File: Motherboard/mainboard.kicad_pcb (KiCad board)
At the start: 4 copper layers, 45.2 x 36 mm, 46 parts, among them IC1 BMX160, J1 Conn_01x01, J2 10118194-0001LF, J28 Conn_01x01, J29 Conn_01x01, J3 Micro_SD_Card, J30 Conn_01x01, J4 xf2m-2415-1a, J5 XF2M-1015-1A, J6 U.FL-R-SMT-1, J7 U.FL-R-SMT-1, SW1 KMR231NG LFS, U1 RFM95W-915S2, U2 ATSAMD51G_TQFN48, U3 DRV8848, U4 TPS82740BSIPR, U5 DRV8848, U6 MAX708RESA-T, U8 RFM95W-915S2

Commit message: branching for fabrication clean-up and review
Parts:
- removed REF**: U.FL_Hirose_U.FL-R-SMT-1_Vertical, Connector_Coaxial:U.FL_Hirose_U.FL-R-SMT-1_Vertical
- R4, R6: moved to B.Cu
- moved R4 31.4 mm to (80.8, 86.4)
- moved R6 31.3 mm to (80.8, 87.6)

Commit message: placement clean-up
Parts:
- added J8: Conn_01x01, TestPoint:TestPoint_Pad_D1.0mm, F.Cu at (104.6, 118.0)
- C6: moved to F.Cu
- J1, J28, J29, J30: footprint custom-footprints:castellated_small_1side -> TestPoint:TestPoint_Pad_D1.0mm
- R7, R8: moved to B.Cu
- moved R7 15.8 mm to (80.9, 80.1)
- moved SW1 15.1 mm to (87.4, 104.9)
- moved R8 13.7 mm to (80.8, 81.4)
- moved C6 11.3 mm to (95.4, 103.0), turned to 90 degrees
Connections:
- net PA04 renamed Net-(U2-Pad9)
- net PA07 renamed Net-(U2-Pad12)
- net PA21 renamed Net-(U2-Pad30)
- net PA22 renamed Net-(U2-Pad31)
- net PA23 renamed Net-(U2-Pad32)

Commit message: placement getting closer
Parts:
- added FID1: Fiducial, custom-footprints:Fiducial_1mm_Silkscreen, F.Cu at (77.6, 76.1)
- added FID2: Fiducial, custom-footprints:Fiducial_1mm_Silkscreen, F.Cu at (77.6, 107.1)
- added FID3: Fiducial, custom-footprints:Fiducial_1mm_Silkscreen, F.Cu at (120.8, 76.1)
- added FID4: Fiducial, custom-footprints:Fiducial_1mm_Silkscreen, F.Cu at (120.8, 106.6)
- C10, C11, C12, C13, C14, C9, R2, R4, R6, R7, R8: moved to F.Cu
- J4, U6: moved to B.Cu
- moved J30 38.5 mm to (84.6, 93.6)
- moved R5 36.5 mm to (80.0, 95.1), turned to 0 degrees
- moved J28 35.1 mm to (82.0, 96.1)
- moved J29 34.7 mm to (82.0, 93.6)
- moved J1 33.0 mm to (87.1, 96.1)
- moved J8 29.7 mm to (84.6, 96.1)
- moved C10 27.7 mm to (87.4, 89.7)
- moved C11 27.6 mm to (89.6, 89.7)
- moved C9 27.6 mm to (88.5, 89.7)
- moved U3 23.5 mm to (88.6, 89.2), turned to 0 degrees
- moved C12 22.3 mm to (88.7, 82.1), turned to 270 degrees
- moved C13 22.3 mm to (90.1, 82.1), turned to 90 degrees
- moved C14 22.3 mm to (87.3, 82.1), turned to 270 degrees
- moved U5 19.3 mm to (88.5, 82.5)
- moved U6 14.0 mm to (88.8, 103.8), turned to 0 degrees
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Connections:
- net CS_RF1 renamed RF1_CS
- net CS_RF2 renamed RF2_CS
- net Net-(U1-Pad15) renamed RF2_IO1
- net RF_CS renamed Net-(U2-Pad19)
- J4 pad 1: SCL2 -> SDA2
- J4 pad 2: SDA2 -> SCL2
- U2 pad 21: RF_RST -> Net-(U2-Pad21)
- U2 pad 22: RF_BUSY -> Net-(U2-Pad22)
- U2 pad 23: RF_DIO3 -> Net-(U2-Pad23)
- U2 pad 24: CS_CAM -> Net-(U2-Pad24)
- U2 pad 27: CS_IMU -> Net-(U2-Pad27)
- U2 pad 29: EN_CAM -> Net-(U2-Pad29)
- U2 pad 38: RF_DIO2 -> Net-(U2-Pad38)
- U2 pad 39: RF_DIO1 -> Net-(U2-Pad39)
- U2 pad 47: RF_DIO0 -> Net-(U2-Pad47)
- U5 pad 1: MXZ_EN -> MY_EN
- U5 pad 10: MINZ_2 -> Net-(U5-Pad10)
- U5 pad 15: MINX_2 -> MINY_2
- U5 pad 16: MINX_1 -> MINY_1
- U5 pad 2: MINX_1 -> MOY_1
- U5 pad 4: MINX_2 -> MOY_2
- U5 pad 5: MOZ_2 -> Net-(U5-Pad5)
- U5 pad 7: MOZ_1 -> Net-(U5-Pad7)
- U5 pad 8: DXZ_FAULT -> DY_FAULT
- U5 pad 9: MINZ_1 -> Net-(U5-Pad9)
- U8 pad 11: RF_DIO3 -> Net-(U8-Pad11)
- U8 pad 12: RF_BUSY -> RF1_BUSY
- U8 pad 14: RF_DIO0 -> Net-(U8-Pad14)
- U8 pad 15: RF_DIO1 -> RF1_IO1
- U8 pad 16: RF_DIO2 -> Net-(U8-Pad16)
- U8 pad 6: RF_RST -> RF1_RST
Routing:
- net SCL2: track 0.00 -> 15.3 mm, vias 0 -> 2
- net SDA2: track 0.00 -> 15.2 mm, vias 0 -> 2
- net /USB+: track 1.12 -> 12.2 mm, vias 1 -> 2
- net /USB-: track 1.13 -> 12.1 mm, vias 1 -> 2
- net Net-(U2-Pad31): track 0.00 -> 1.56 mm, vias 0 -> 1
- net Net-(U2-Pad27): track 0.00 -> 1.56 mm, vias 0 -> 1
- net Net-(U2-Pad29): track 0.00 -> 1.55 mm, vias 0 -> 1
- net Net-(U2-Pad30): track 0.00 -> 0.80 mm, vias 0 -> 1
- net Net-(U2-Pad28): track 0.00 -> 0.79 mm, vias 0 -> 1
- net Net-(U2-Pad32): track 0.00 -> 0.79 mm, vias 0 -> 1

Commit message: placement roughed-in & routing planned
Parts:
- moved C4 6.87 mm to (113.0, 95.4), turned to 90 degrees
- moved IC1 2.65 mm to (109.0, 95.0)
- moved C2 2.38 mm to (95.3, 104.3)
- moved C8 1.44 mm to (109.0, 98.3), turned to 0 degrees
- moved J5 0.51 mm to (115.1, 98.8)
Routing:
- net SCK: track 0.00 -> 52.8 mm, vias 0 -> 6
- net MISO: track 0.00 -> 46.6 mm, vias 0 -> 6
- net MOSI: track 0.00 -> 46.0 mm, vias 0 -> 6
- net Net-(U2-Pad27): track 1.56 -> 18.6 mm
- net Net-(U2-Pad32): track 0.79 -> 15.7 mm
- net Net-(U2-Pad29): track 1.55 -> 15.1 mm
- net Net-(U2-Pad30): track 0.80 -> 13.4 mm
- net Net-(U2-Pad31): track 1.56 -> 14.1 mm
- net Net-(U2-Pad28): track 0.79 -> 9.97 mm
- net Net-(U2-Pad24): track 0.00 -> 8.29 mm, vias 0 -> 1
- net Net-(U2-Pad21): track 0.00 -> 7.70 mm, vias 0 -> 1
- net Net-(U2-Pad22): track 0.00 -> 4.56 mm, vias 0 -> 1
- net +3V3: track 0.00 -> 3.64 mm, vias 0 -> 5
- net Net-(U2-Pad23): track 0.00 -> 3.32 mm, vias 0 -> 1
- net Net-(U2-Pad16): track 0.00 -> 1.57 mm, vias 0 -> 1
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
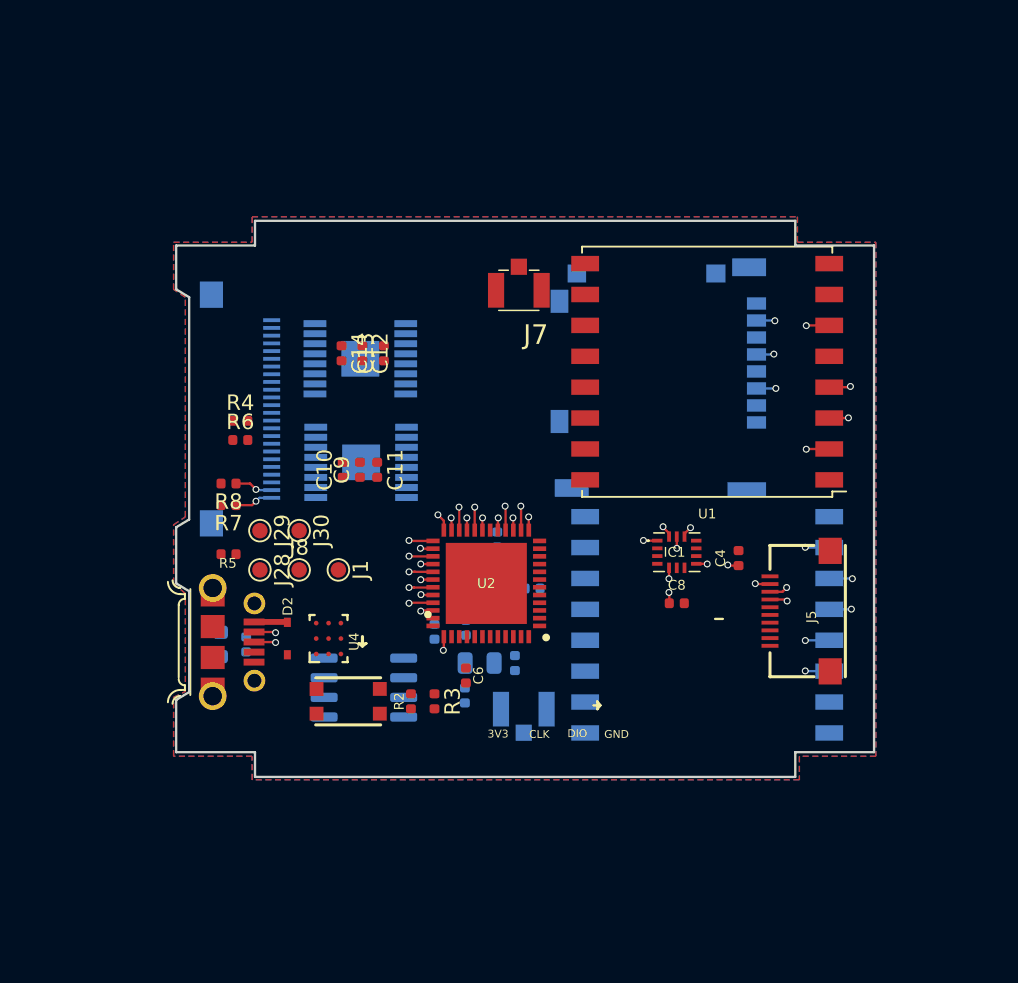
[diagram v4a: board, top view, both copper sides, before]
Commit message: rearranging for power distrobution
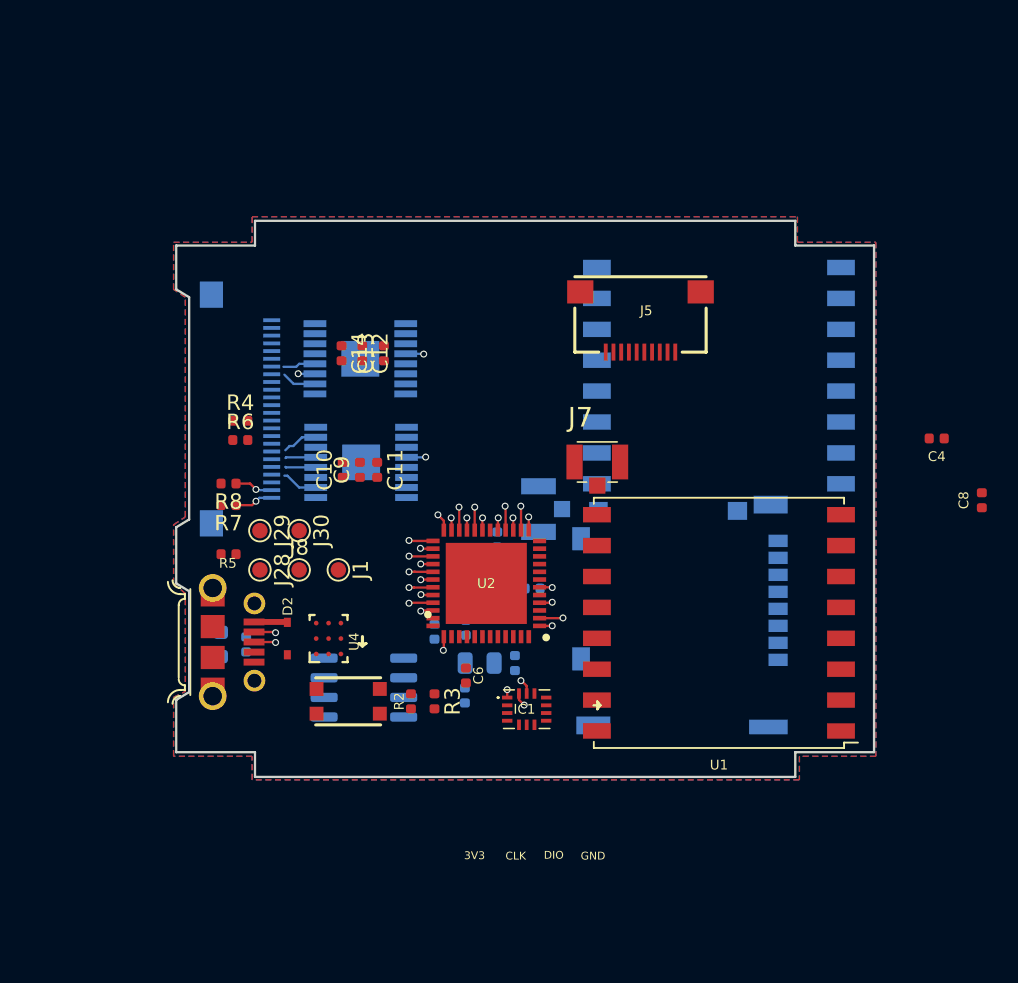
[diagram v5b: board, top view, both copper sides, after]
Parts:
- moved C8 20.8 mm to (128.8, 91.6), turned to 90 degrees
- moved J5 18.7 mm to (106.7, 82.0), turned to 180 degrees
- moved U1 16.3 mm to (111.8, 99.6)
- moved U8 16.1 mm to (111.8, 83.6)
- moved J3 15.4 mm to (110.0, 99.1)
- moved C4 15.0 mm to (125.9, 87.6), turned to 180 degrees
- moved IC1 14.1 mm to (99.3, 105.2)
- moved J6 13.0 mm to (100.1, 92.2), turned to 270 degrees
- moved J7 12.2 mm to (103.9, 89.2), turned to 0 degrees
- moved FID4 5.40 mm to (115.8, 108.7)
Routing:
- net (no net): track 0.00 -> 70.3 mm
- net SCK: track 52.8 -> 13.9 mm, vias 6 -> 2
- net MISO: track 46.6 -> 12.6 mm, vias 6 -> 2
- net MOSI: track 46.0 -> 14.0 mm, vias 6 -> 2
- net BATT_P: track 0.00 -> 17.2 mm, vias 0 -> 2
- net MOX_1: track 0.00 -> 2.34 mm
- net MOZ_1: track 0.00 -> 2.31 mm
- net MOY_1: track 0.00 -> 2.22 mm
- net MOY_2: track 0.00 -> 2.12 mm
- net MOZ_2: track 0.00 -> 1.98 mm
- net MOX_2: track 0.00 -> 1.98 mm
- net RF1_CS: track 1.56 -> 0.00 mm, vias 1 -> 0
- net RF1_RST: track 1.56 -> 0.00 mm, vias 1 -> 0
- net SCL1: track 0.00 -> 1.52 mm, vias 0 -> 1
- net RF2_RST: track 1.49 -> 0.00 mm, vias 1 -> 0
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
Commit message: much cleaner SPI and BATT_P layout
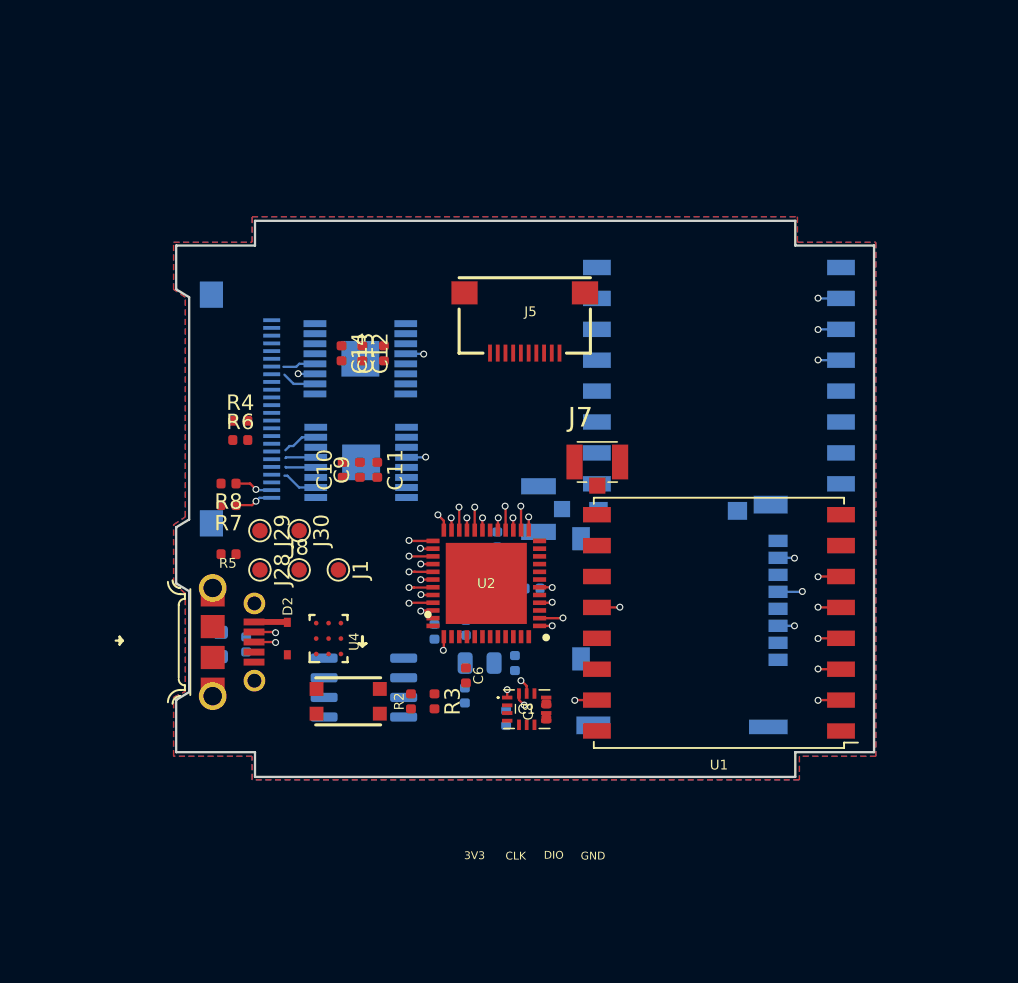
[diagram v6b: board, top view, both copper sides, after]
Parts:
- C4: moved to B.Cu
- moved C4 33.2 mm to (98.0, 105.7), turned to 90 degrees
- moved C8 31.3 mm to (100.6, 105.3)
- moved J5 7.49 mm to (99.2, 82.1)
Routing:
- net (no net): track 70.3 -> 0.00 mm
- net MISO: track 12.6 -> 44.5 mm, vias 2 -> 5
- net MOSI: track 14.0 -> 41.3 mm, vias 2 -> 5
- net SCK: track 13.9 -> 37.3 mm, vias 2 -> 5
- net RF2_BUSY: track 0.00 -> 1.49 mm, vias 0 -> 1
- net RF2_CS: track 0.00 -> 1.49 mm, vias 0 -> 1
- net RF2_RST: track 0.00 -> 1.49 mm, vias 0 -> 1
- net RF2_IO1: track 0.00 -> 1.44 mm, vias 0 -> 1

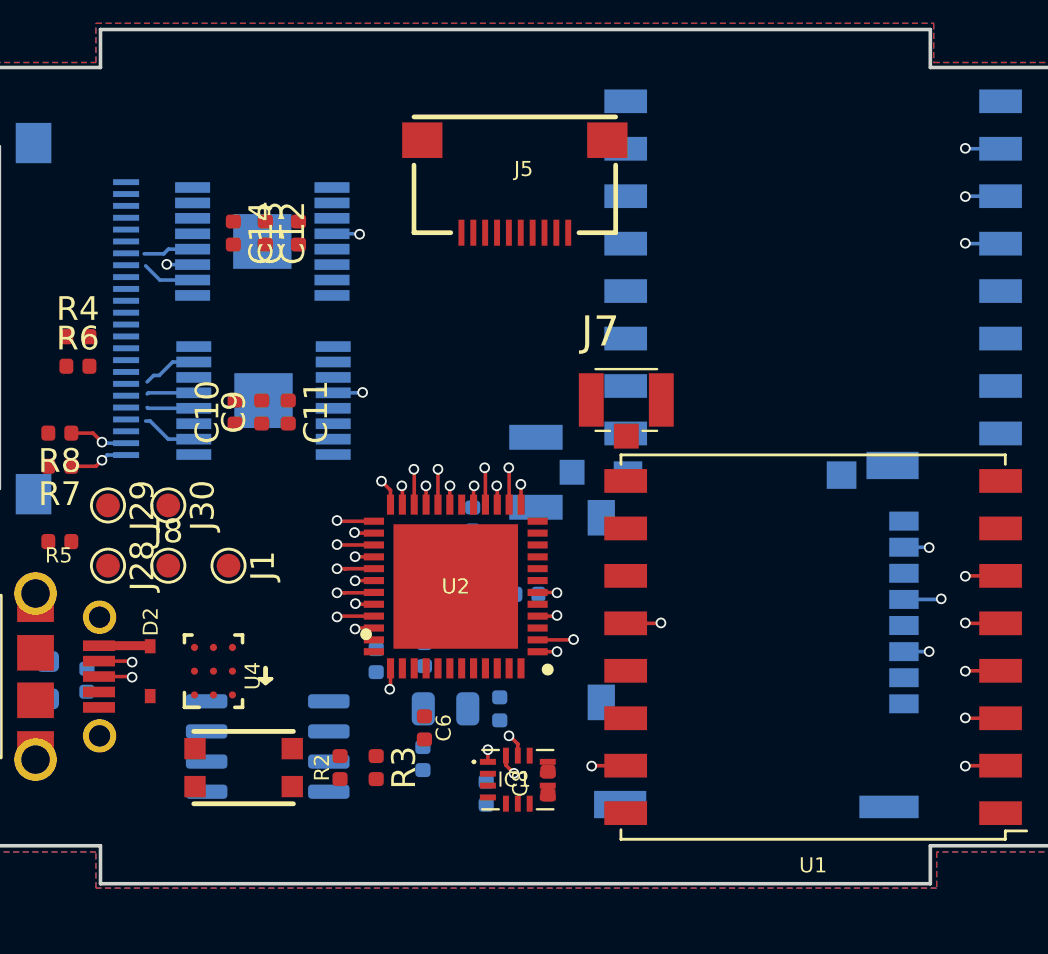
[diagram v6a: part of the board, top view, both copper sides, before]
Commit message: ~75% routed
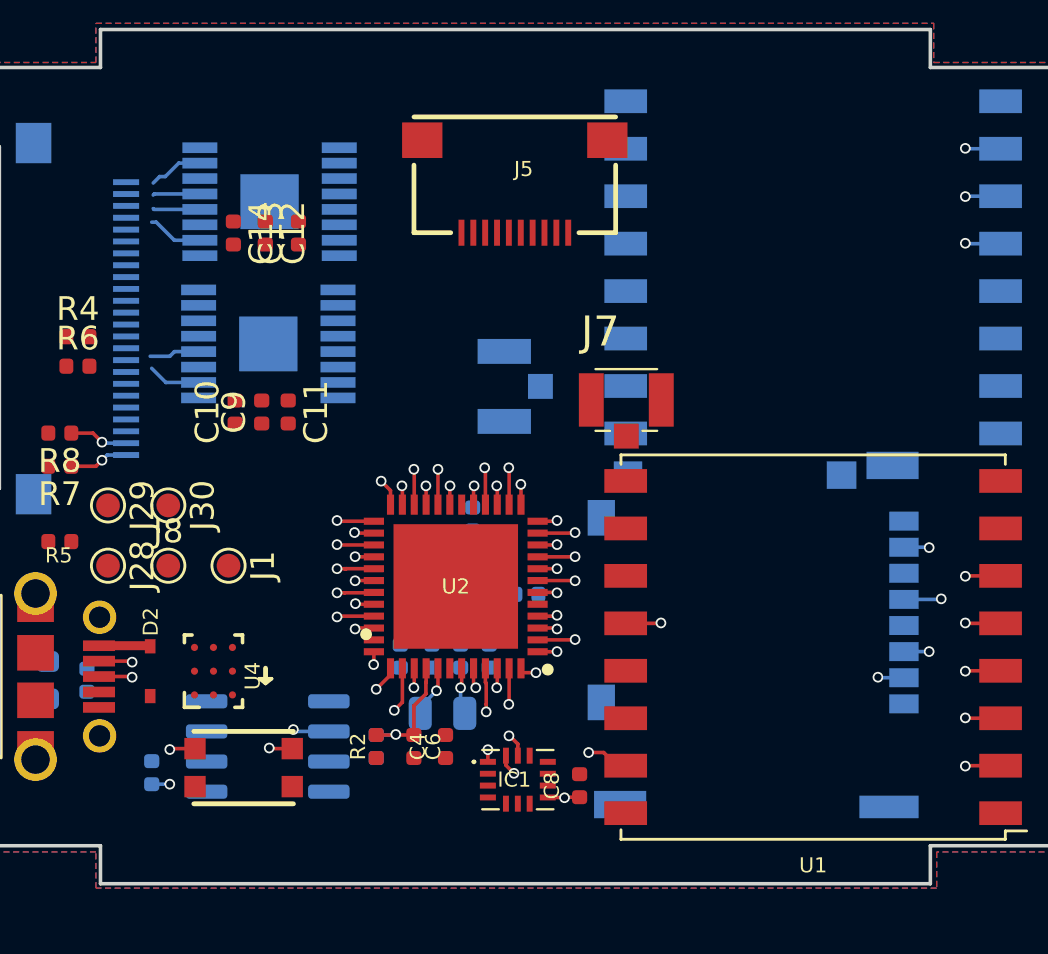
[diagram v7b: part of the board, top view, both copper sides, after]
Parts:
- added C16: 0.1uF, Capacitor_SMD:C_0402_1005Metric, B.Cu at (83.9, 104.9)
- C4: moved to F.Cu
- R3: moved to B.Cu
- moved U3 8.39 mm to (88.8, 80.8)
- moved C2 4.60 mm to (96.9, 99.9), turned to 90 degrees
- moved U5 4.33 mm to (88.8, 86.8)
- moved J6 3.86 mm to (98.7, 88.6)
- moved C4 2.61 mm to (96.3, 103.8)
- moved C1 2.27 mm to (98.1, 99.9), turned to 90 degrees
- moved R2 1.76 mm to (93.3, 103.8)
- moved C8 1.34 mm to (101.9, 105.4)
- moved C15 1.03 mm to (94.4, 100.0)
- moved C6 0.90 mm to (94.9, 103.8)
- moved R3 0.89 mm to (93.3, 103.8)
- moved C5 0.32 mm to (95.7, 99.9), turned to 90 degrees
- moved L1 0.23 mm to (96.1, 102.4)
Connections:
- R1 pad 2: /LED1 -> Net-(R1-Pad2)
- U2 pad 48: /LED1 -> Net-(U2-Pad48)
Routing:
- net MISO: track 44.5 -> 75.7 mm
- net SCK: track 37.3 -> 66.6 mm
- net MOSI: track 41.3 -> 70.5 mm
- net SCL1: track 1.52 -> 23.4 mm
- net SDA1: track 0.82 -> 21.9 mm
- net RF2_CS: track 1.49 -> 20.0 mm
- net ~RESET: track 0.00 -> 17.3 mm, vias 0 -> 3
- net Net-(U2-Pad47): track 0.00 -> 17.0 mm, vias 0 -> 1
- net RF2_RST: track 1.49 -> 17.5 mm
- net Net-(U2-Pad22): track 4.56 -> 15.3 mm
- net Net-(U2-Pad28): track 10.2 -> 19.5 mm
- net Net-(U2-Pad21): track 7.70 -> 16.2 mm
- net Net-(U2-Pad23): track 3.32 -> 11.5 mm
- net /SWCLK: track 0.00 -> 7.14 mm, vias 0 -> 1
- net /SWDIO: track 0.00 -> 6.42 mm, vias 0 -> 1
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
